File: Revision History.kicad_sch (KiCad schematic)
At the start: 0 parts

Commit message: Finished 65% of schematics
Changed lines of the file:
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@@
 (kicad_sch
-	(version 20231120)
+	(version 20250114)
 	(generator "eeschema")
-	(generator_version "8.0")
+	(generator_version "9.0")
 	(paper "A4")
 	(title_block
@@
 		(company "${COMPANY}")
 	)
-	(polyline
-		(pts
-			(xy 19.05 31.75) (xy 19.05 149.86)
-		)
-		(stroke
-			(width 0.635)
-			(type default)
-			(color 0 0 0 1)
-		)
-	)
-	(polyline
-		(pts
-			(xy 85.09 31.75) (xy 85.09 149.86)
-		)
-		(stroke
-			(width 0.635)
-			(type default)
-			(color 0 0 0 1)
-		)
-	)
-	(polyline
-		(pts
-			(xy 85.09 31.75) (xy 85.09 149.86)
-		)
-		(stroke
-			(width 0.635)
-			(type default)
-			(color 0 0 0 1)
-		)
-	)
-	(polyline
-		(pts
-			(xy 151.13 31.75) (xy 151.13 149.86)
-		)
-		(stroke
-			(width 0.635)
-			(type default)
-			(color 0 0 0 1)
-		)
-	)
-	(polyline
-		(pts
-			(xy 19.05 31.75) (xy 19.05 149.86)
-		)
-		(stroke
-			(width 0.635)
-			(type default)
-			(color 0 0 0 1)
-		)
-	)
-	(polyline
-		(pts
-			(xy 217.17 31.75) (xy 217.17 149.86)
-		)
-		(stroke
-			(width 0.635)
-			(type default)
-			(color 0 0 0 1)
-		)
-	)
 	(text_box "- _________________________________\n\n- _________________________________\n\n- _________________________________\n\n- _________________________________\n\n- _________________________________\n\n- _________________________________\n\n- _________________________________\n\n- _________________________________\n\n- _________________________________\n\n- _________________________________\n\n- _________________________________\n\n- _________________________________\n\n- _________________________________\n\n- _________________________________\n\n- _________________________________\n\n- _________________________________\n\n- _________________________________"
 		(exclude_from_sim no)
 		(at 220.98 40.64 0)
 		(size 58.42 115.57)
+		(margins 1.4287 1.4287 1.4287 1.4287)
 		(stroke
 			(width -0.0001)
@@
 		(at 86.36 31.75 0)
 		(size 57.15 7.62)
+		(margins 1.4287 1.4287 1.4287 1.4287)
 		(stroke
 			(width -0.0001)
@@
 		(at 80.01 16.51 0)
 		(size 137.16 12.7)
+		(margins 4.4999 4.4999 4.4999 4.4999)
 		(stroke
 			(width -0.0001)
@@
 		(at 152.4 31.75 0)
 		(size 57.15 7.62)
+		(margins 1.4287 1.4287 1.4287 1.4287)
 		(stroke
 			(width -0.0001)
@@
 		(at 22.86 40.64 0)
 		(size 58.42 115.57)
+		(margins 1.4287 1.4287 1.4287 1.4287)
 		(stroke
 			(width -0.0001)
@@
 		(at 154.94 40.64 0)
 		(size 58.42 115.57)
+		(margins 1.4287 1.4287 1.4287 1.4287)
 		(stroke
 			(width -0.0001)
@@
 		(at 20.32 31.75 0)
 		(size 57.15 7.62)
+		(margins 1.4287 1.4287 1.4287 1.4287)
 		(stroke
 			(width -0.0001)
@@
 		(at 88.9 40.64 0)
 		(size 58.42 115.57)
+		(margins 1.4287 1.4287 1.4287 1.4287)
 		(stroke
 			(width -0.0001)
@@
 		(at 218.44 31.75 0)
 		(size 57.15 7.62)
-		(stroke
-			(width -0.0001)
-			(type default)
-		)
-		(fill
-			(type none)
-		)
-		(effects
-			(font
-				(face "Arial")
-				(size 1.905 1.905)
-				(thickness 0.254)
-				(bold yes)
-			)
-			(justify left top)
-		)
-	)
+		(margins 1.4287 1.4287 1.4287 1.4287)
+		(stroke
+			(width -0.0001)
+			(type default)
+		)
+		(fill
+			(type none)
+		)
+		(effects
+			(font
+				(face "Arial")
+				(size 1.905 1.905)
+				(thickness 0.254)
+				(bold yes)
+			)
+			(justify left top)
+		)
+	)
+	(polyline
+		(pts
+			(xy 19.05 31.75) (xy 19.05 149.86)
+		)
+		(stroke
+			(width 0.635)
+			(type default)
+			(color 0 0 0 1)
+		)
+	)
+	(polyline
+		(pts
+			(xy 85.09 31.75) (xy 85.09 149.86)
+		)
+		(stroke
+			(width 0.635)
+			(type default)
+			(color 0 0 0 1)
+		)
+	)
+	(polyline
+		(pts
+			(xy 85.09 31.75) (xy 85.09 149.86)
+		)
+		(stroke
+			(width 0.635)
+			(type default)
+			(color 0 0 0 1)
+		)
+	)
+	(polyline
+		(pts
+			(xy 151.13 31.75) (xy 151.13 149.86)
+		)
+		(stroke
+			(width 0.635)
+			(type default)
+			(color 0 0 0 1)
+		)
+	)
+	(polyline
+		(pts
+			(xy 19.05 31.75) (xy 19.05 149.86)
+		)
+		(stroke
+			(width 0.635)
+			(type default)
+			(color 0 0 0 1)
+		)
+	)
+	(polyline
+		(pts
+			(xy 217.17 31.75) (xy 217.17 149.86)
+		)
+		(stroke
+			(width 0.635)
+			(type default)
+			(color 0 0 0 1)
+		)
+	)

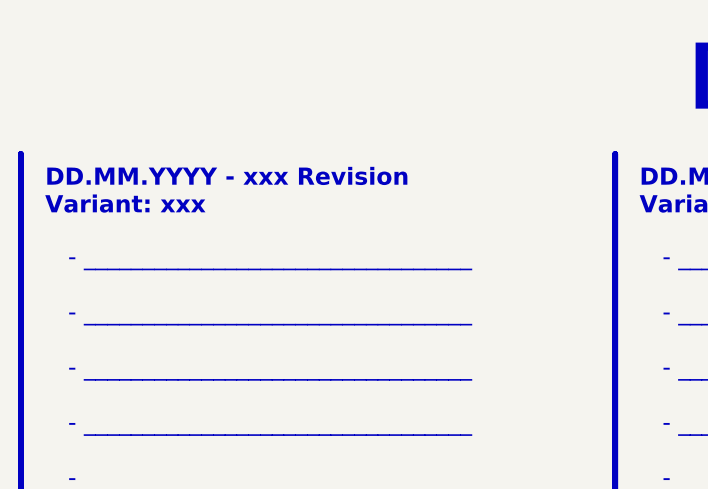
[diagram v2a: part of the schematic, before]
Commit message: Checked MCU pinout, cleaned shematic, advanced the ioc file
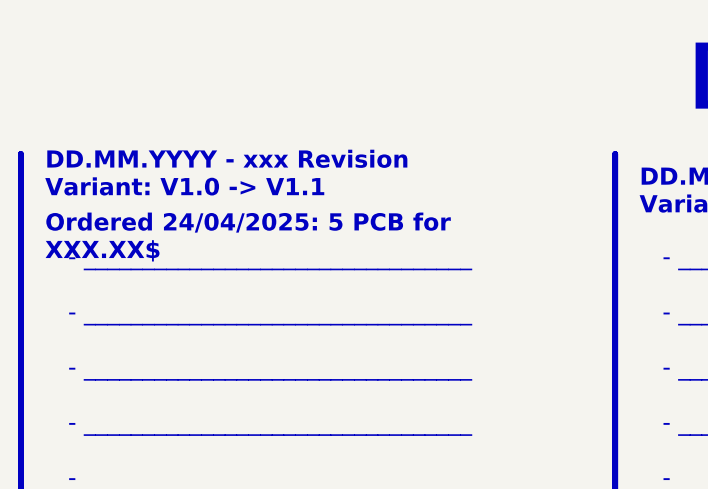
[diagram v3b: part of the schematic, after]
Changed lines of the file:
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@@
 	(title_block
 		(title "Revision History")
-		(date "2025-04-05")
+		(date "2025-04-21")
 		(rev "${REVISION}")
 		(company "${COMPANY}")
@@
 		)
 	)
+	(text_box "DD.MM.YYYY - xxx Revision\nVariant: V1.0 -> V1.1"
+		(exclude_from_sim no)
+		(at 20.32 29.845 0)
+		(size 57.15 7.62)
+		(margins 1.4287 1.4287 1.4287 1.4287)
+		(stroke
+			(width -0.0001)
+			(type solid)
+		)
+		(fill
+			(type none)
+		)
+		(effects
+			(font
+				(face "Arial")
+				(size 1.905 1.905)
+				(thickness 0.254)
+				(bold yes)
+			)
+			(justify left top)
+		)
+	)
+	(text_box "- _________________________________\n\n- _________________________________\n\n- _________________________________\n\n- _________________________________\n\n- _________________________________\n\n- _________________________________\n\n- _________________________________\n\n- _________________________________\n\n- _________________________________\n\n- _________________________________\n\n- _________________________________\n\n- _________________________________\n\n- _________________________________\n\n- _________________________________\n\n- _________________________________\n\n- _________________________________\n\n- _________________________________"
+		(exclude_from_sim no)
+		(at 88.9 40.64 0)
+		(size 58.42 115.57)
+		(margins 1.4287 1.4287 1.4287 1.4287)
+		(stroke
+			(width -0.0001)
+			(type default)
+		)
+		(fill
+			(type none)
+		)
+		(effects
+			(font
+				(face "Arial")
+				(size 1.905 1.905)
+				(color 0 0 0 1)
+			)
+			(justify left top)
+		)
+	)
 	(text_box "DD.MM.YYYY - xxx Revision\nVariant: xxx"
 		(exclude_from_sim no)
-		(at 20.32 31.75 0)
-		(size 57.15 7.62)
-		(margins 1.4287 1.4287 1.4287 1.4287)
-		(stroke
-			(width -0.0001)
-			(type default)
-		)
-		(fill
-			(type none)
-		)
-		(effects
-			(font
-				(face "Arial")
-				(size 1.905 1.905)
-				(thickness 0.254)
-				(bold yes)
-			)
-			(justify left top)
-		)
-	)
-	(text_box "- _________________________________\n\n- _________________________________\n\n- _________________________________\n\n- _________________________________\n\n- _________________________________\n\n- _________________________________\n\n- _________________________________\n\n- _________________________________\n\n- _________________________________\n\n- _________________________________\n\n- _________________________________\n\n- _________________________________\n\n- _________________________________\n\n- _________________________________\n\n- _________________________________\n\n- _________________________________\n\n- _________________________________"
-		(exclude_from_sim no)
-		(at 88.9 40.64 0)
-		(size 58.42 115.57)
-		(margins 1.4287 1.4287 1.4287 1.4287)
-		(stroke
-			(width -0.0001)
-			(type default)
-		)
-		(fill
-			(type none)
-		)
-		(effects
-			(font
-				(face "Arial")
-				(size 1.905 1.905)
-				(color 0 0 0 1)
-			)
-			(justify left top)
-		)
-	)
-	(text_box "DD.MM.YYYY - xxx Revision\nVariant: xxx"
-		(exclude_from_sim no)
 		(at 218.44 31.75 0)
 		(size 57.15 7.62)
@@
 			)
 			(justify left top)
+		)
+	)
+	(text_box "Ordered 24/04/2025: 5 PCB for XXX.XX$"
+		(exclude_from_sim no)
+		(at 20.32 36.83 0)
+		(size 62.23 7.62)
+		(margins 1.4287 1.4287 1.4287 1.4287)
+		(stroke
+			(width -0.0001)
+			(type solid)
+		)
+		(fill
+			(type none)
+		)
+		(effects
+			(font
+				(face "Arial")
+				(size 1.905 1.905)
+				(thickness 0.254)
+				(bold yes)
+				(color 194 0 0 1)
+			)
+			(justify left top)

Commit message: Final version, cleaned and ordered as is
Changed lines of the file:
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@@
 	(title_block
 		(title "Revision History")
-		(date "2025-04-21")
+		(date "2025-04-24")
 		(rev "${REVISION}")
 		(company "${COMPANY}")
@@
 		)
 	)
-	(text_box "Ordered 24/04/2025: 5 PCB for XXX.XX$"
+	(text_box "Ordered 24/04/2025: 5 PCB for 232.48$"
 		(exclude_from_sim no)
 		(at 20.32 36.83 0)

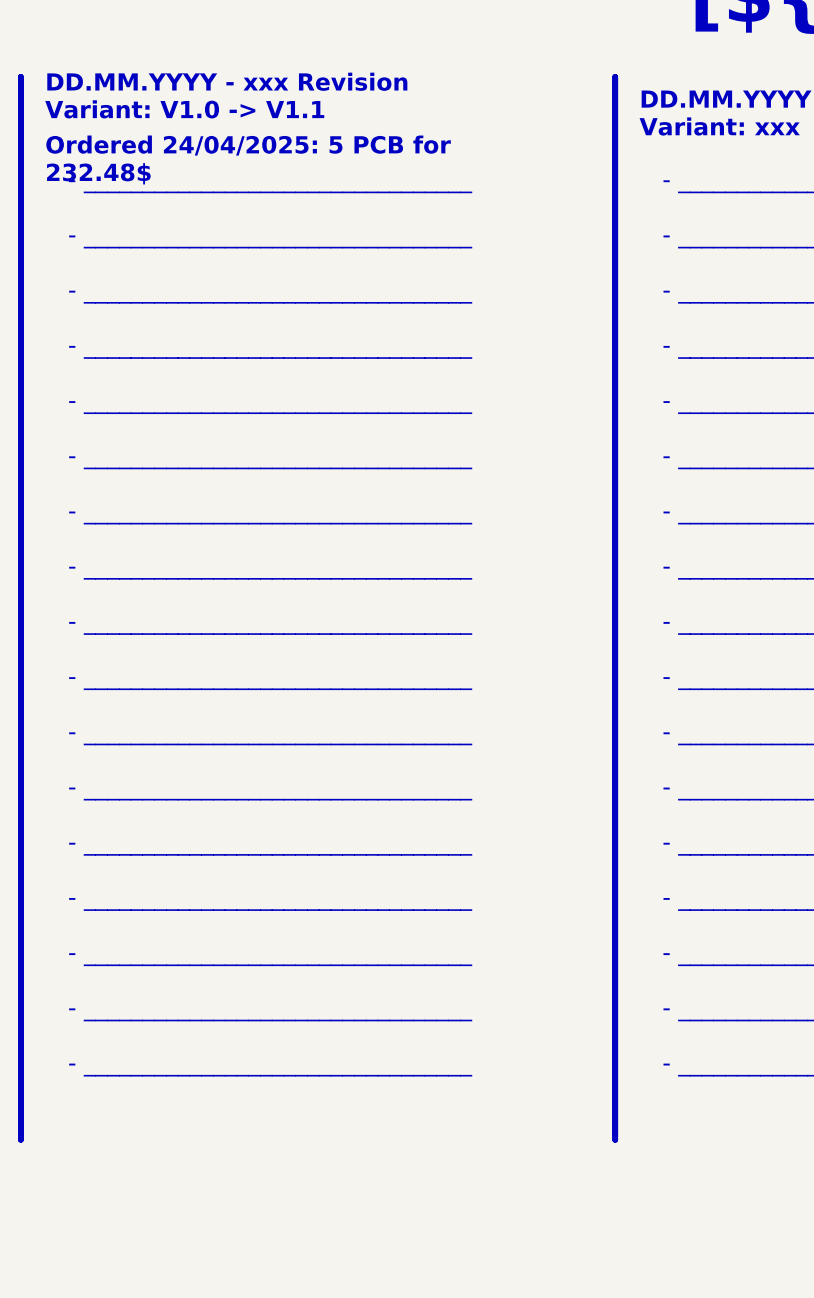
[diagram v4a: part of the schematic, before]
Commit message: Cleaned repo, remnamed folder, added latest version of drv8214 library
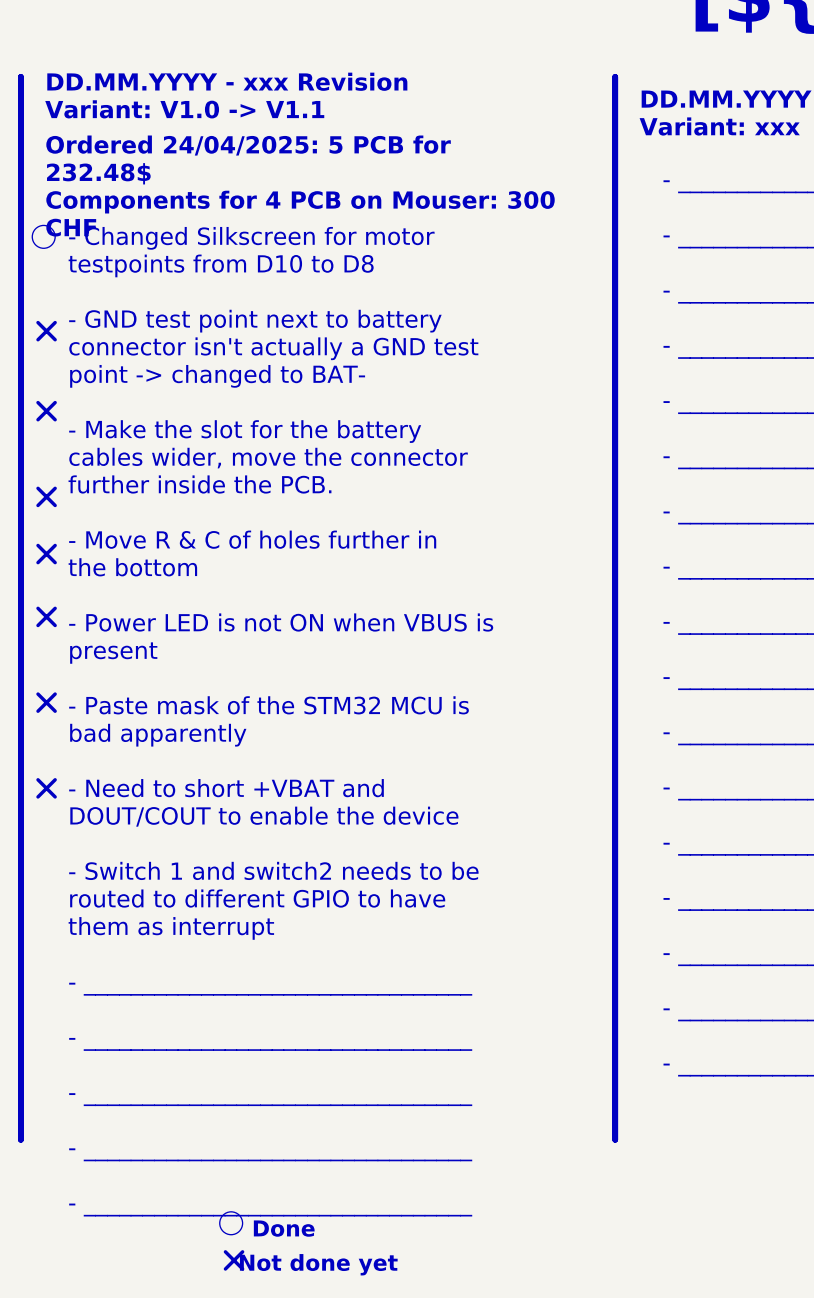
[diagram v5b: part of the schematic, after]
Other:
- note added: "Done"
- note added: "Not done yet"
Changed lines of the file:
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@@
 		(company "${COMPANY}")
+	)
+	(circle
+		(center 42.418 159.131)
+		(radius 1.27)
+		(stroke
+			(width -0.0001)
+			(type solid)
+		)
+		(fill
+			(type color)
+			(color 0 255 0 1)
+		)
+	)
+	(circle
+		(center 21.59 49.53)
+		(radius 1.27)
+		(stroke
+			(width -0.0001)
+			(type solid)
+		)
+		(fill
+			(type color)
+			(color 0 255 0 1)
+		)
+	)
+	(text "Done"
+		(exclude_from_sim no)
+		(at 48.26 160.02 0)
+		(effects
+			(font
+				(size 1.778 1.778)
+				(thickness 0.3556)
+				(bold yes)
+				(color 0 0 0 1)
+			)
+		)
+	)
+	(text "Not done yet"
+		(exclude_from_sim no)
+		(at 52.07 163.83 0)
+		(effects
+			(font
+				(size 1.778 1.778)
+				(thickness 0.3556)
+				(bold yes)
+				(color 0 0 0 1)
+			)
+		)
 	)
 	(text_box "- _________________________________\n\n- _________________________________\n\n- _________________________________\n\n- _________________________________\n\n- _________________________________\n\n- _________________________________\n\n- _________________________________\n\n- _________________________________\n\n- _________________________________\n\n- _________________________________\n\n- _________________________________\n\n- _________________________________\n\n- _________________________________\n\n- _________________________________\n\n- _________________________________\n\n- _________________________________\n\n- _________________________________"
@@
 		)
 	)
-	(text_box "- _________________________________\n\n- _________________________________\n\n- _________________________________\n\n- _________________________________\n\n- _________________________________\n\n- _________________________________\n\n- _________________________________\n\n- _________________________________\n\n- _________________________________\n\n- _________________________________\n\n- _________________________________\n\n- _________________________________\n\n- _________________________________\n\n- _________________________________\n\n- _________________________________\n\n- _________________________________\n\n- _________________________________"
-		(exclude_from_sim no)
-		(at 22.86 40.64 0)
+	(text_box "- Changed Silkscreen for motor testpoints from D10 to D8\n\n- GND test point next to battery connector isn't actually a GND test point -> changed to BAT-\n\n- Make the slot for the battery cables wider, move the connector further inside the PCB.\n\n- Move R & C of holes further in the bottom\n\n- Power LED is not ON when VBUS is present\n\n- Paste mask of the STM32 MCU is bad apparently\n\n- Need to short +VBAT and DOUT/COUT to enable the device\n\n- Switch 1 and switch2 needs to be routed to different GPIO to have them as interrupt\n\n- _________________________________\n\n- _________________________________\n\n- _________________________________\n\n- _________________________________\n\n- _________________________________"
+		(exclude_from_sim no)
+		(at 22.86 46.99 0)
 		(size 58.42 115.57)
 		(margins 1.4287 1.4287 1.4287 1.4287)
 		(stroke
 			(width -0.0001)
-			(type default)
+			(type solid)
 		)
 		(fill
@@
 		)
 	)
-	(text_box "Ordered 24/04/2025: 5 PCB for 232.48$"
+	(text_box "Ordered 24/04/2025: 5 PCB for 232.48$\nComponents for 4 PCB on Mouser: 300 CHF"
 		(exclude_from_sim no)
 		(at 20.32 36.83 0)
@@
 	(polyline
 		(pts
+			(xy 22.86 111.76) (xy 20.955 109.855)
+		)
+		(stroke
+			(width 0.381)
+			(type solid)
+			(color 255 0 0 1)
+		)
+	)
+	(polyline
+		(pts
+			(xy 22.86 69.85) (xy 20.955 67.945)
+		)
+		(stroke
+			(width 0.381)
+			(type solid)
+			(color 255 0 0 1)
+		)
+	)
+	(polyline
+		(pts
+			(xy 20.955 60.96) (xy 22.86 59.055)
+		)
+		(stroke
+			(width 0.381)
+			(type solid)
+			(color 255 0 0 1)
+		)
+	)
+	(polyline
+		(pts
+			(xy 43.688 164.211) (xy 41.783 162.306)
+		)
+		(stroke
+			(width 0.381)
+			(type solid)
+			(color 255 0 0 1)
+		)
+	)
+	(polyline
+		(pts
+			(xy 22.86 102.235) (xy 20.955 100.33)
+		)
+		(stroke
+			(width 0.381)
+			(type solid)
+			(color 255 0 0 1)
+		)
+	)
+	(polyline
+		(pts
 			(xy 19.05 31.75) (xy 19.05 149.86)
 		)
@@
 	(polyline
 		(pts
+			(xy 22.86 85.725) (xy 20.955 83.82)
+		)
+		(stroke
+			(width 0.381)
+			(type solid)
+			(color 255 0 0 1)
+		)
+	)
+	(polyline
+		(pts
+			(xy 22.86 92.71) (xy 20.955 90.805)
+		)
+		(stroke
+			(width 0.381)
+			(type solid)
+			(color 255 0 0 1)
+		)
+	)
+	(polyline
+		(pts
+			(xy 20.955 111.76) (xy 22.86 109.855)
+		)
+		(stroke
+			(width 0.381)
+			(type solid)
+			(color 255 0 0 1)
+		)
+	)
+	(polyline
+		(pts
 			(xy 85.09 31.75) (xy 85.09 149.86)
 		)
@@
 	(polyline
 		(pts
+			(xy 20.955 79.375) (xy 22.86 77.47)
+		)
+		(stroke
+			(width 0.381)
+			(type solid)
+			(color 255 0 0 1)
+		)
+	)
+	(polyline
+		(pts
+			(xy 41.783 164.211) (xy 43.688 162.306)
+		)
+		(stroke
+			(width 0.381)
+			(type solid)
+			(color 255 0 0 1)
+		)
+	)
+	(polyline
+		(pts
 			(xy 151.13 31.75) (xy 151.13 149.86)
 		)
@@
 	(polyline
 		(pts
+			(xy 20.955 92.71) (xy 22.86 90.805)
+		)
+		(stroke
+			(width 0.381)
+			(type solid)
+			(color 255 0 0 1)
+		)
+	)
+	(polyline
+		(pts
 			(xy 19.05 31.75) (xy 19.05 149.86)
 		)
@@
 		)
 	)
+	(polyline
+		(pts
+			(xy 22.86 79.375) (xy 20.955 77.47)
+		)
+		(stroke
+			(width 0.381)
+			(type solid)
+			(color 255 0 0 1)
+		)
+	)
+	(polyline
+		(pts
+			(xy 20.955 102.235) (xy 22.86 100.33)
+		)
+		(stroke
+			(width 0.381)
+			(type solid)
+			(color 255 0 0 1)
+		)
+	)
+	(polyline
+		(pts
+			(xy 20.955 85.725) (xy 22.86 83.82)
+		)
+		(stroke
+			(width 0.381)
+			(type solid)
+			(color 255 0 0 1)
+		)
+	)
+	(polyline
+		(pts
+			(xy 20.955 69.85) (xy 22.86 67.945)
+		)
+		(stroke
+			(width 0.381)
+			(type solid)
+			(color 255 0 0 1)
+		)
+	)
+	(polyline
+		(pts
+			(xy 22.86 60.96) (xy 20.955 59.055)
+		)
+		(stroke
+			(width 0.381)
+			(type solid)
+			(color 255 0 0 1)
+		)
+	)
